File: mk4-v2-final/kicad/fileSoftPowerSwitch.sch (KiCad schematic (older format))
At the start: 11 parts, among them Q26 Q_NMOS_GDS, Q3 2N3904, Q4 2N3904

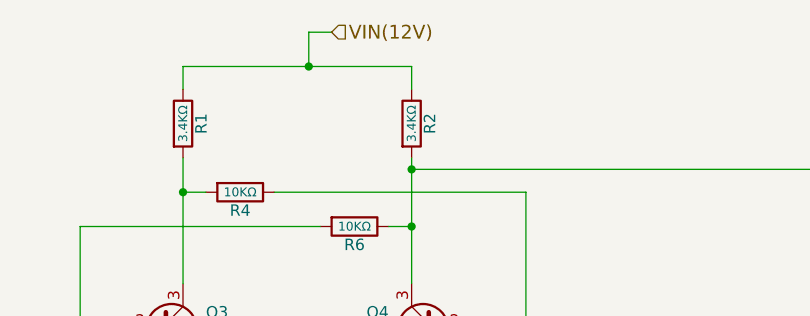
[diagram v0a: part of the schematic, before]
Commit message: got most of the screw terminals planned out in schem
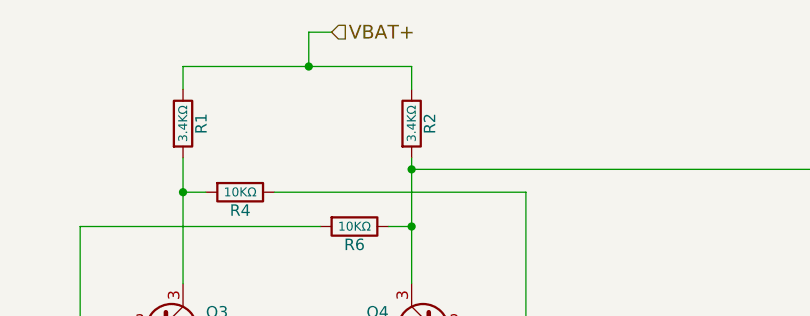
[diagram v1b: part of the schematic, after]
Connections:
- net VIN(12V) renamed VBAT+
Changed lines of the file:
@@
 $Descr A4 11693 8268
 encoding utf-8
-Sheet 44 51
+Sheet 44 54
 Title ""
 Date ""
@@
 GND
 Text HLabel 5050 2350 2    60   Input ~ 0
-VIN(12V)
+VBAT+
 $Comp
 L R R3

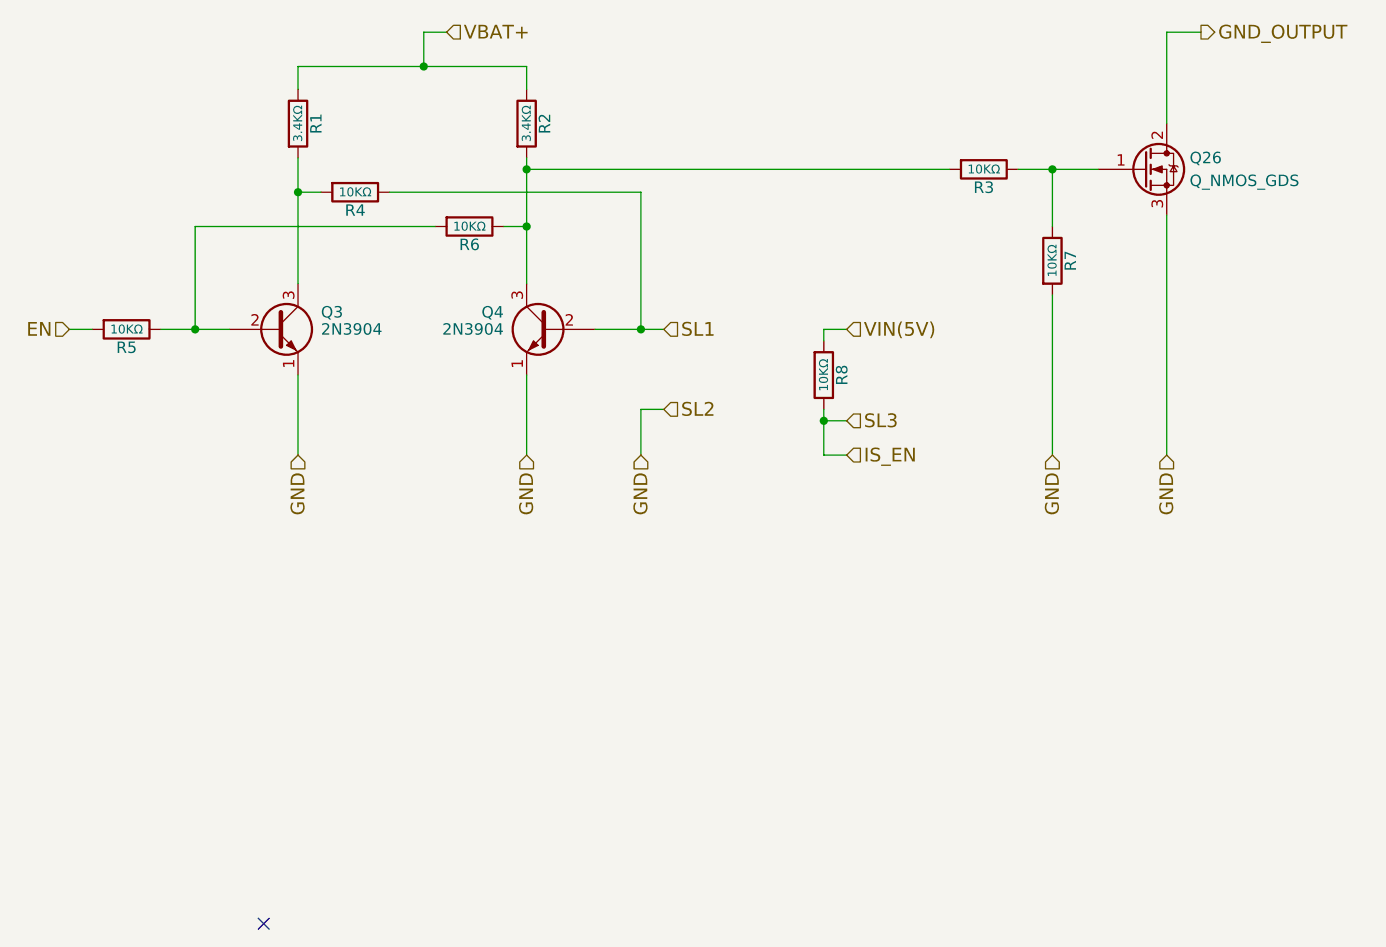
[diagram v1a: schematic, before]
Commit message: added headnight diodes, I don't think software control of them is going to be possible
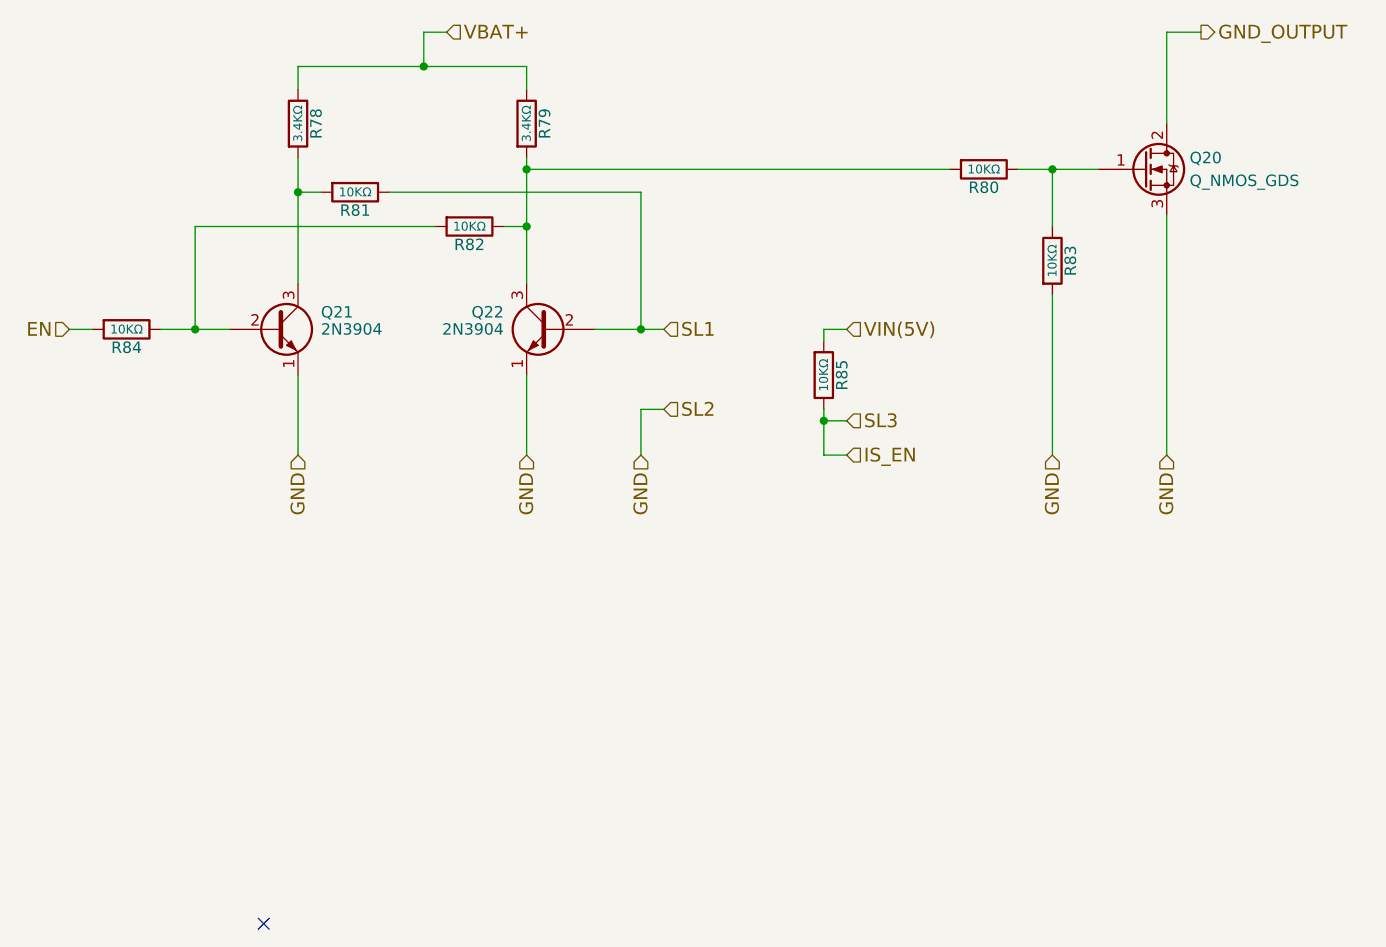
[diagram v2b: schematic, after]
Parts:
- renumbered Q26 to Q20, Q3 to Q21, Q4 to Q22, R1 to R78, R2 to R79, R3 to R80, R4 to R81, R6 to R82, R7 to R83, R5 to R84, R8 to R85
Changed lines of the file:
@@
 $EndDescr
 $Comp
-L R R1
+L R R78
 U 1 1 5A25E2DD
 P 4400 2750
-F 0 "R1" V 4480 2750 50  0000 C CNN
+F 0 "R78" V 4480 2750 50  0000 C CNN
 F 1 "3.4KΩ" V 4400 2750 39  0000 C CNN
 F 2 "Resistors_THT:R_Axial_DIN0207_L6.3mm_D2.5mm_P10.16mm_Horizontal" V 4330 2750 50  0001 C CNN
@@
 $EndComp
 $Comp
-L R R4
+L R R81
 U 1 1 5A25E2E4
 P 4650 3050
-F 0 "R4" V 4730 3050 50  0000 C CNN
+F 0 "R81" V 4730 3050 50  0000 C CNN
 F 1 "10KΩ" V 4650 3050 39  0000 C CNN
 F 2 "Resistors_THT:R_Axial_DIN0207_L6.3mm_D2.5mm_P10.16mm_Horizontal" V 4580 3050 50  0001 C CNN
@@
 $EndComp
 $Comp
-L 2N3904 Q3
+L 2N3904 Q21
 U 1 1 5A25E2EB
 P 4300 3650
-F 0 "Q3" H 4500 3725 50  0000 L CNN
+F 0 "Q21" H 4500 3725 50  0000 L CNN
 F 1 "2N3904" H 4500 3650 50  0000 L CNN
 F 2 "TO_SOT_Packages_THT:TO-92_Molded_Narrow" H 4500 3575 50  0001 L CIN
@@
 $EndComp
 $Comp
-L R R6
+L R R82
 U 1 1 5A25E2F2
 P 5150 3200
-F 0 "R6" V 5230 3200 50  0000 C CNN
+F 0 "R82" V 5230 3200 50  0000 C CNN
 F 1 "10KΩ" V 5150 3200 39  0000 C CNN
 F 2 "Resistors_THT:R_Axial_DIN0207_L6.3mm_D2.5mm_P10.16mm_Horizontal" V 5080 3200 50  0001 C CNN
@@
 $EndComp
 $Comp
-L R R2
+L R R79
 U 1 1 5A25E2F9
 P 5400 2750
-F 0 "R2" V 5480 2750 50  0000 C CNN
+F 0 "R79" V 5480 2750 50  0000 C CNN
 F 1 "3.4KΩ" V 5400 2750 39  0000 C CNN
 F 2 "Resistors_THT:R_Axial_DIN0207_L6.3mm_D2.5mm_P10.16mm_Horizontal" V 5330 2750 50  0001 C CNN
@@
 $EndComp
 $Comp
-L 2N3904 Q4
+L 2N3904 Q22
 U 1 1 5A25E300
 P 5500 3650
-F 0 "Q4" H 5700 3725 50  0000 L CNN
+F 0 "Q22" H 5700 3725 50  0000 L CNN
 F 1 "2N3904" H 5700 3650 50  0000 L CNN
 F 2 "TO_SOT_Packages_THT:TO-92_Molded_Narrow" H 5700 3575 50  0001 L CIN
@@
 VBAT+
 $Comp
-L R R3
+L R R80
 U 1 1 5A25E312
 P 7400 2950
-F 0 "R3" V 7480 2950 50  0000 C CNN
+F 0 "R80" V 7480 2950 50  0000 C CNN
 F 1 "10KΩ" V 7400 2950 39  0000 C CNN
 F 2 "Resistors_THT:R_Axial_DIN0207_L6.3mm_D2.5mm_P10.16mm_Horizontal" V 7330 2950 50  0001 C CNN
@@
 $EndComp
 $Comp
-L R R7
+L R R83
 U 1 1 5A25E319
 P 7700 3350
-F 0 "R7" V 7780 3350 50  0000 C CNN
+F 0 "R83" V 7780 3350 50  0000 C CNN
 F 1 "10KΩ" V 7700 3350 39  0000 C CNN
 F 2 "Resistors_THT:R_Axial_DIN0207_L6.3mm_D2.5mm_P10.16mm_Horizontal" V 7630 3350 50  0001 C CNN
@@
 SL3
 $Comp
-L R R8
+L R R85
 U 1 1 5A25E32E
 P 6700 3850
-F 0 "R8" V 6780 3850 50  0000 C CNN
+F 0 "R85" V 6780 3850 50  0000 C CNN
 F 1 "10KΩ" V 6700 3850 39  0000 C CNN
 F 2 "Resistors_THT:R_Axial_DIN0207_L6.3mm_D2.5mm_P10.16mm_Horizontal" V 6630 3850 50  0001 C CNN
@@
 VIN(5V)
 $Comp
-L R R5
+L R R84
 U 1 1 5A25E339
 P 3650 3650
-F 0 "R5" V 3730 3650 50  0000 C CNN
+F 0 "R84" V 3730 3650 50  0000 C CNN
 F 1 "10KΩ" V 3650 3650 39  0000 C CNN
 F 2 "Resistors_THT:R_Axial_DIN0207_L6.3mm_D2.5mm_P10.16mm_Horizontal" V 3580 3650 50  0001 C CNN
@@
 NoConn ~ 4250 6250
 $Comp
-L Q_NMOS_GDS Q26
+L Q_NMOS_GDS Q20
 U 1 1 5A2EEE12
 P 8100 2950
-F 0 "Q26" H 8300 3000 50  0000 L CNN
+F 0 "Q20" H 8300 3000 50  0000 L CNN
 F 1 "Q_NMOS_GDS" H 8300 2900 50  0000 L CNN
 F 2 "TO_SOT_Packages_THT:TO-220-3_Vertical" H 8300 3050 50  0001 C CNN
